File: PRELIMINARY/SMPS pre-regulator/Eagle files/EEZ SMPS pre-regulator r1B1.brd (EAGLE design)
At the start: 60 x 100 mm, 108 parts, among them IC1 LTC3864, IC2 Si8610BC-B-IS, IC3 MC79L05, IC4 MC78L05, IC5 LM5574, IC6 LP2951SO8, IC7 TLC555, Q1 SUD19P06-60, Q2 MMBT5401, Q3 2N7002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

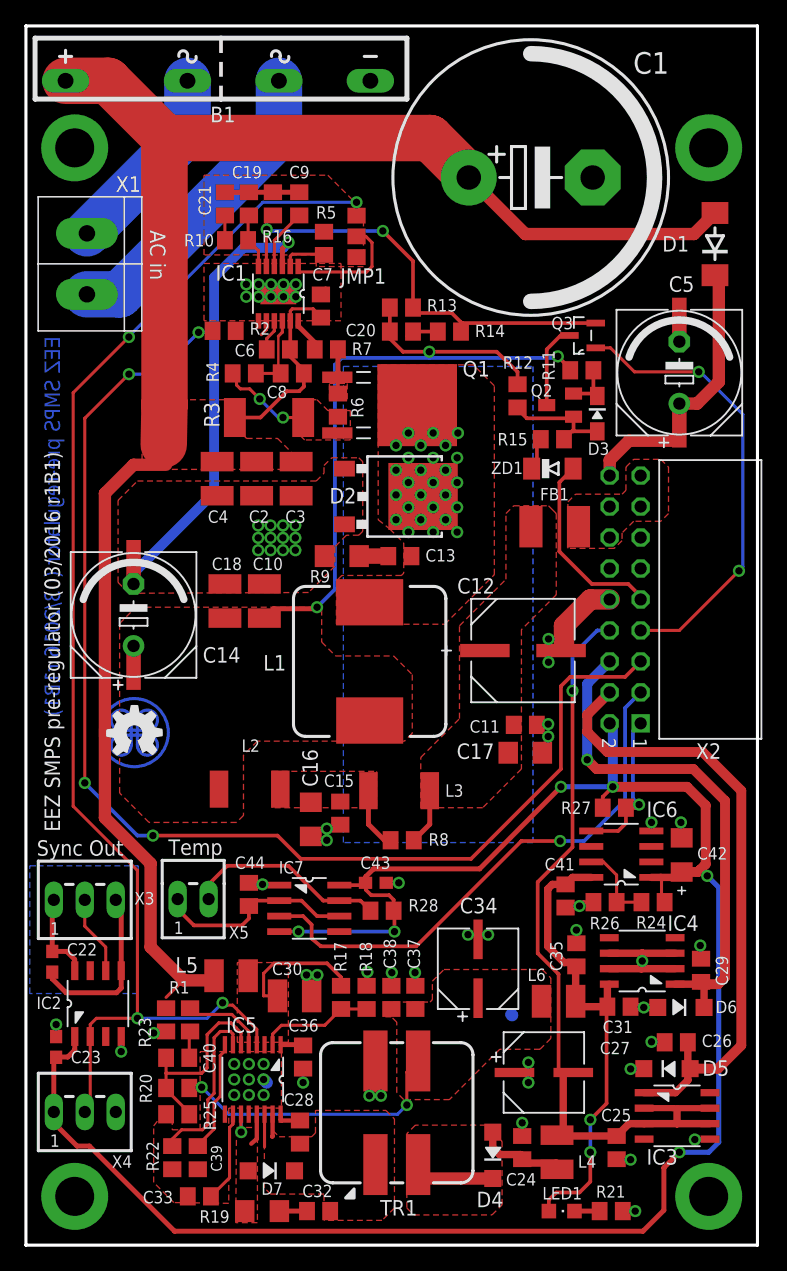
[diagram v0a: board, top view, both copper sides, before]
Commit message: Few PCB layout correction for SMPS pre-regulator r1B1
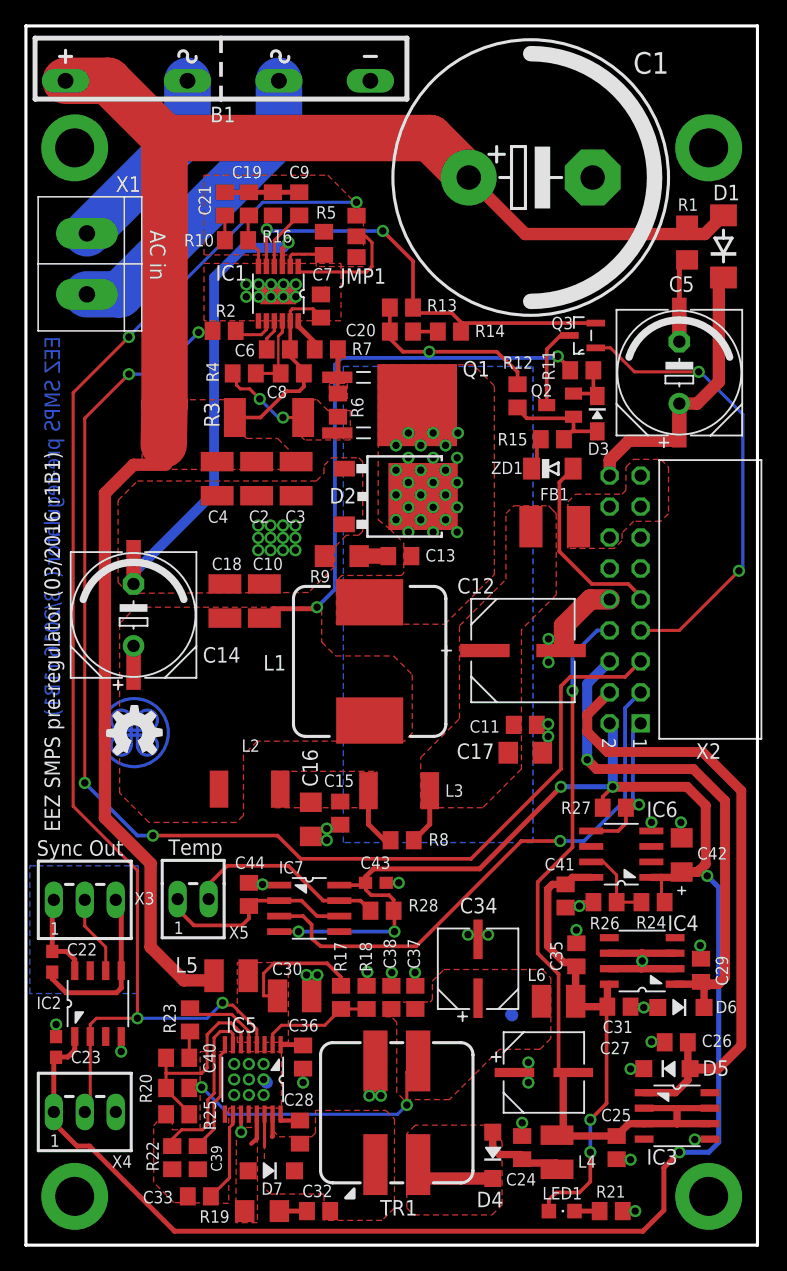
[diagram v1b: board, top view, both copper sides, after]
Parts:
- R1: device rcl:R0805 -> rcl:R1206
- moved R1 76.8 mm to (54.2, 82.2)
- moved D1 0.72 mm to (57.2, 81.9)
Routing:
- net GND: track 61.6 -> 66.0 mm, vias 67 -> 66
- net SD: track 1.30 -> 3.72 mm
- net DC_OUT: track 155.8 -> 155.1 mm

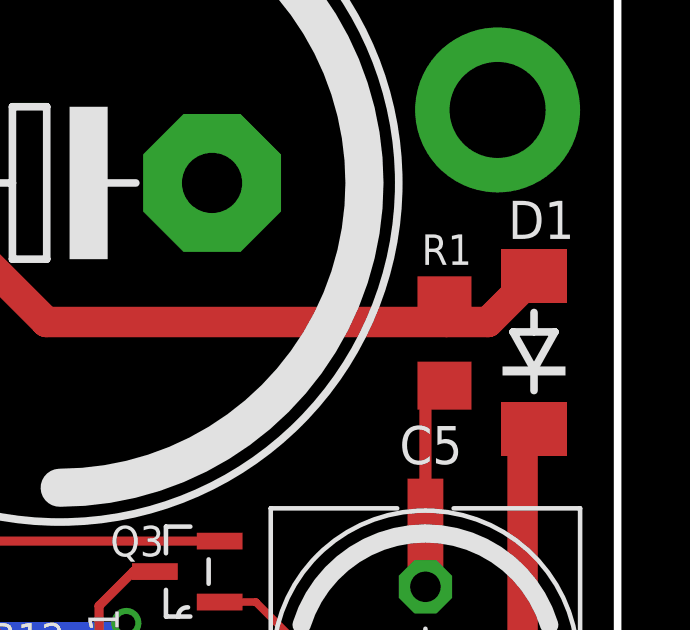
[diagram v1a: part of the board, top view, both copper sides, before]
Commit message: SMPS pre-regulator small corrections
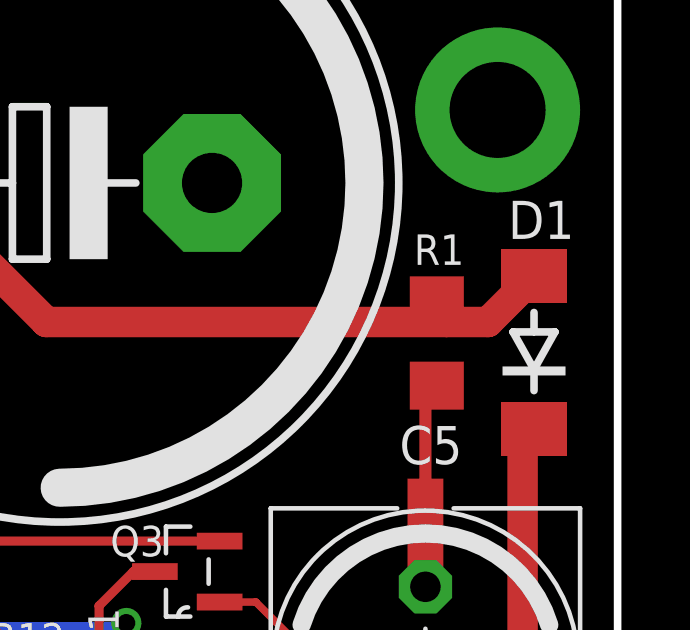
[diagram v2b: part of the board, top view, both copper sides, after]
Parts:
- C20: value 47n -> 47p
- moved R1 0.25 mm to (54.0, 82.2)
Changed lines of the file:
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@@
 <layer number="17" name="Pads" color="14" fill="1" visible="yes" active="yes"/>
 <layer number="18" name="Vias" color="14" fill="1" visible="yes" active="yes"/>
-<layer number="19" name="Unrouted" color="6" fill="1" visible="no" active="yes"/>
+<layer number="19" name="Unrouted" color="6" fill="1" visible="yes" active="yes"/>
 <layer number="20" name="Dimension" color="15" fill="1" visible="yes" active="yes"/>
 <layer number="21" name="tPlace" color="7" fill="1" visible="yes" active="yes"/>
 <layer number="22" name="bPlace" color="7" fill="1" visible="no" active="yes"/>
-<layer number="23" name="tOrigins" color="15" fill="1" visible="no" active="yes"/>
+<layer number="23" name="tOrigins" color="15" fill="1" visible="yes" active="yes"/>
 <layer number="24" name="bOrigins" color="15" fill="1" visible="no" active="yes"/>
 <layer number="25" name="tNames" color="7" fill="1" visible="yes" active="yes"/>
@@
 <layer number="27" name="tValues" color="10" fill="1" visible="no" active="yes"/>
 <layer number="28" name="bValues" color="7" fill="1" visible="no" active="yes"/>
-<layer number="29" name="tStop" color="7" fill="3" visible="no" active="yes"/>
+<layer number="29" name="tStop" color="7" fill="3" visible="yes" active="yes"/>
 <layer number="30" name="bStop" color="7" fill="6" visible="no" active="yes"/>
 <layer number="31" name="tCream" color="7" fill="4" visible="no" active="yes"/>
@@
 <layer number="49" name="Reference" color="7" fill="1" visible="no" active="yes"/>
 <layer number="50" name="dxf" color="7" fill="1" visible="no" active="no"/>
-<layer number="51" name="tDocu" color="14" fill="1" visible="yes" active="yes"/>
+<layer number="51" name="tDocu" color="14" fill="1" visible="no" active="yes"/>
 <layer number="52" name="bDocu" color="7" fill="1" visible="no" active="no"/>
 <layer number="53" name="tGND_GNDA" color="7" fill="9" visible="no" active="no"/>
@@
 <layer number="56" name="wert" color="7" fill="1" visible="no" active="no"/>
 <layer number="57" name="tCAD" color="7" fill="1" visible="no" active="no"/>
-<layer number="90" name="Modules" color="7" fill="1" visible="no" active="yes"/>
+<layer number="90" name="Modules" color="7" fill="1" visible="yes" active="yes"/>
 <layer number="91" name="Nets" color="2" fill="1" visible="no" active="no"/>
 <layer number="92" name="Busses" color="1" fill="1" visible="no" active="no"/>
@@
 <layer number="123" name="tTestmark" color="7" fill="1" visible="no" active="no"/>
 <layer number="124" name="bTestmark" color="7" fill="1" visible="no" active="no"/>
-<layer number="125" name="_tNames" color="14" fill="1" visible="no" active="yes"/>
+<layer number="125" name="_tNames" color="14" fill="1" visible="yes" active="yes"/>
 <layer number="126" name="_bNames" color="7" fill="1" visible="no" active="no"/>
 <layer number="127" name="_tValues" color="7" fill="1" visible="no" active="no"/>
@@
 <text x="41.402" y="69.596" size="1.016" layer="125" ratio="10">Q2</text>
 <text x="43.0911" y="75.1205" size="1.016" layer="125" ratio="10" rot="SR0">Q3</text>
-<text x="53.467" y="84.836" size="1.016" layer="125" ratio="10">R1</text>
+<text x="53.213" y="84.836" size="1.016" layer="125" ratio="10">R1</text>
 <text x="15.5575" y="76.1365" size="1.016" layer="125" ratio="10">R2</text>
 <text x="14.605" y="69.1515" size="1.27" layer="125" ratio="10" rot="R270">R3</text>
@@
 <text x="16.637" y="25.146" size="1.016" layer="125" ratio="10">X5</text>
 <text x="40.767" y="64.262" size="1.016" layer="125" ratio="10" rot="R180">ZD1</text>
+<wire x1="0" y1="93" x2="32" y2="93" width="0.1" layer="90"/>
+<wire x1="32" y1="93" x2="32" y2="83" width="0.1" layer="90"/>
+<wire x1="32" y1="83" x2="51" y2="83" width="0.1" layer="90"/>
+<wire x1="51" y1="83" x2="51" y2="93" width="0.1" layer="90"/>
+<wire x1="51" y1="93" x2="60" y2="93" width="0.1" layer="90"/>
+<wire x1="60" y1="93" x2="60" y2="76" width="0.1" layer="90"/>
+<wire x1="60" y1="76" x2="45" y2="76" width="0.1" layer="90"/>
+<wire x1="45" y1="76" x2="45" y2="10" width="0.1" layer="90"/>
+<wire x1="45" y1="10" x2="60" y2="10" width="0.1" layer="90"/>
+<wire x1="60" y1="10" x2="60" y2="0" width="0.1" layer="90"/>
+<wire x1="60" y1="0" x2="0" y2="0" width="0.1" layer="90"/>
+<wire x1="0" y1="0" x2="0" y2="9" width="0.1" layer="90"/>
+<wire x1="0" y1="9" x2="18" y2="9" width="0.1" layer="90"/>
+<wire x1="18" y1="9" x2="18" y2="86" width="0.1" layer="90"/>
+<wire x1="0" y1="86" x2="18" y2="86" width="0.1" layer="90"/>
+<wire x1="0" y1="86" x2="0" y2="93" width="0.1" layer="90"/>
 </plain>
 <attributes>
@@
 <attribute name="VALUE" x="33.909" y="74.422" size="1.016" layer="27" ratio="10"/>
 </element>
-<element name="C20" library="rcl" package="C0805" value="47n" x="30.7975" y="74.93" smashed="yes">
+<element name="C20" library="rcl" package="C0805" value="47p" x="30.7975" y="74.93" smashed="yes">
 <attribute name="NAME" x="28.702" y="75.565" size="1.016" layer="25" ratio="10" rot="R180"/>
 <attribute name="VALUE" x="32.0675" y="75.3745" size="1.016" layer="27" ratio="10" rot="R180"/>
@@
 <attribute name="VALUE" x="48.9585" y="6.223" size="1.016" layer="27" ratio="10" rot="R90"/>
 </element>
-<element name="R1" library="rcl" package="R1206" value="18K" x="54.229" y="82.2325" smashed="yes" rot="R270">
-<attribute name="NAME" x="53.467" y="84.836" size="1.016" layer="25" ratio="10"/>
-<attribute name="VALUE" x="54.61" y="80.9625" size="1.016" layer="27" ratio="10" rot="R90"/>
+<element name="R1" library="rcl" package="R1206" value="18K" x="53.975" y="82.2325" smashed="yes" rot="R270">
+<attribute name="NAME" x="53.213" y="84.836" size="1.016" layer="25" ratio="10"/>
+<attribute name="VALUE" x="54.356" y="80.9625" size="1.016" layer="27" ratio="10" rot="R90"/>
 </element>
 <element name="R21" library="rcl" package="R0805" value="390R" x="48.006" y="2.794" smashed="yes">
@@
 <element name="C4" library="rcl" package="C1210" value="4u7" x="15.6845" y="62.865" smashed="yes" rot="R270">
 <attribute name="NAME" x="14.9225" y="59.2455" size="1.016" layer="25" ratio="10"/>
-<attribute name="VALUE" x="12.5095" y="64.77" size="1.27" layer="27" rot="R270"/>
+<attribute name="VALUE" x="15.113" y="64.1985" size="1.016" layer="27" ratio="10" rot="R270"/>
 </element>
 </elements>
@@
 <contactref element="C4" pad="2"/>
 <wire x1="53.594" y1="75.6285" x2="53.594" y2="80.1755" width="0.4064" layer="1"/>
-<wire x1="53.594" y1="80.1755" x2="54.229" y2="80.8105" width="0.4064" layer="1"/>
+<wire x1="53.594" y1="80.1755" x2="53.975" y2="80.8105" width="0.4064" layer="1"/>
 <wire x1="8.8265" y1="54.229" x2="8.582" y2="54.229" width="0" layer="19" extent="16-16"/>
 <wire x1="27.94" y1="21.27" x2="27.94" y2="21.2725" width="0" layer="19" extent="1-1"/>
@@
 <wire x1="11.249015625" y1="69.022" x2="11.3665" y2="68.9597" width="0.254" layer="1"/>
 <contactref element="C4" pad="1"/>
-<wire x1="54.229" y1="83.6545" x2="54.229" y2="82.9945" width="0.4064" layer="1"/>
+<wire x1="53.975" y1="83.6545" x2="54.229" y2="82.9945" width="0.4064" layer="1"/>
 <wire x1="54.229" y1="82.9945" x2="54.2925" y2="82.931" width="0.4064" layer="1"/>
 <wire x1="54.2925" y1="82.931" x2="55.6795" y2="82.931" width="1.016" layer="1"/>
